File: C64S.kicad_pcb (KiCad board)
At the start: 2 copper layers, 30.7 x 38.2 mm, 4 parts, among them J1 DATASETTE PORT, J2 DB25_Plug, J3 Barrel_Jack_Switch

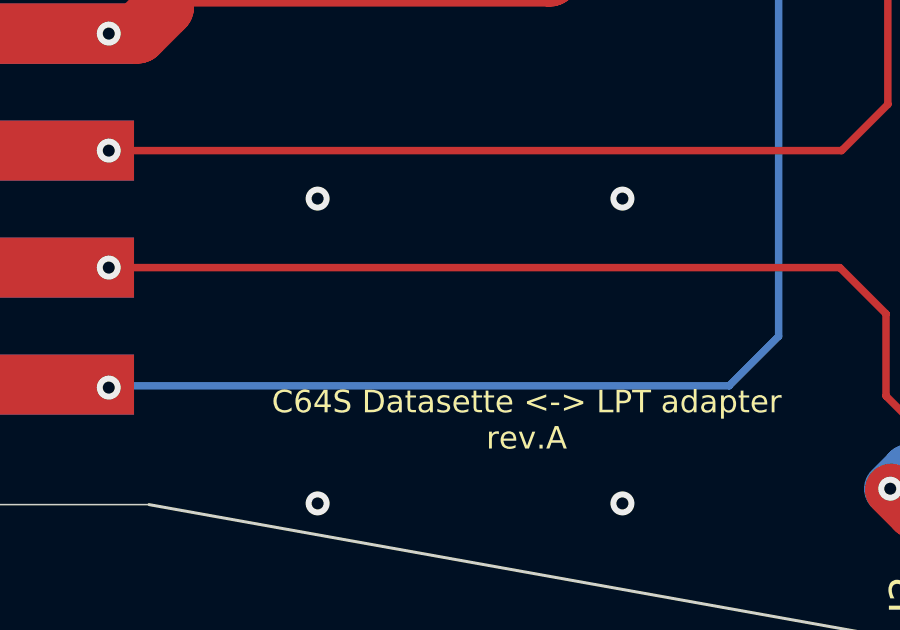
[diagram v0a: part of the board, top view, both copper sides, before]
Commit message: Add LCSC part no's, website address and update schematic
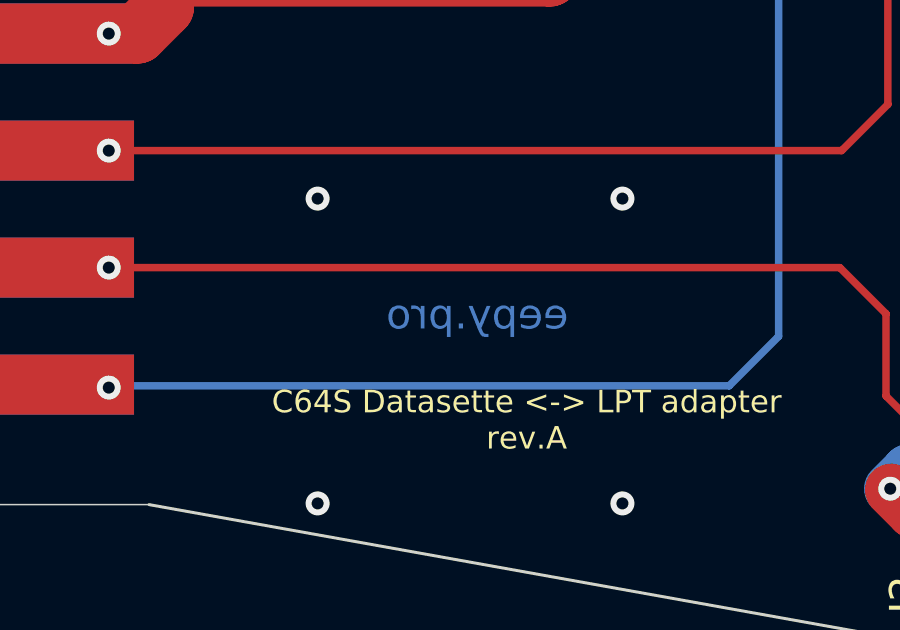
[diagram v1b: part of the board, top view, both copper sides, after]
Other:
- board text added: "eepy.pro"
